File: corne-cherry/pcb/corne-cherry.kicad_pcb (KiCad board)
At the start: 2 copper layers, 152.8 x 91.4 mm, 101 parts, among them J1 MJ-4PP-9, J2 OLED, J3 LED, P1 i2c-pin, P2 i2c-pin, SW1 SW_PUSH, SW10 SW_PUSH, SW11 SW_PUSH, SW12 SW_PUSH, SW13 SW_PUSH, SW14 SW_PUSH, SW15 SW_PUSH, SW16 SW_PUSH, SW17 SW_PUSH, SW18 SW_PUSH, SW19 SW_PUSH, SW2 SW_PUSH, SW20 SW_PUSH, SW21 SW_PUSH, SW22 SW_PUSH, SW3 SW_PUSH, SW4 SW_PUSH, SW5 SW_PUSH, SW6 SW_PUSH, SW7 SW_PUSH, SW8 SW_PUSH, SW9 SW_PUSH, U1 ProMicro

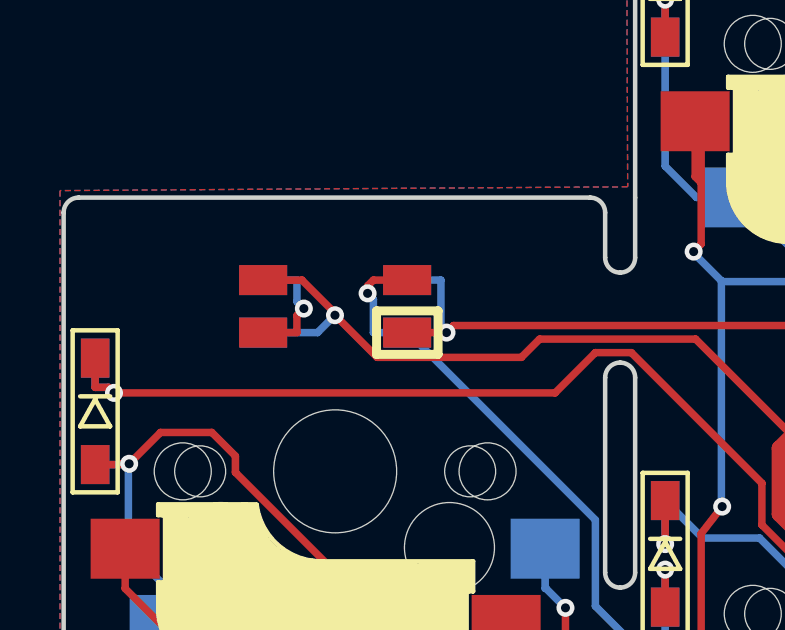
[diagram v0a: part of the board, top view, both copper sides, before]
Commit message: fixed LED holes in corne-cherry 2.1
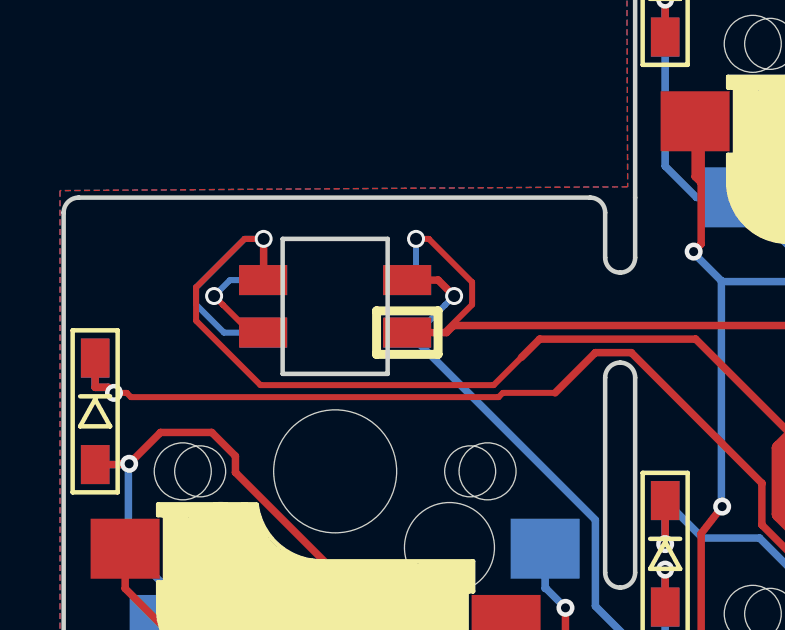
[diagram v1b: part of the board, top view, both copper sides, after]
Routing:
- net GND: track 855.0 -> 867.4 mm
- net VCC: track 784.8 -> 789.1 mm
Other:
- outline, holes or cut-outs redrawn

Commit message: Clean
Clean up
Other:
- net class Default removed
- net class Power removed
